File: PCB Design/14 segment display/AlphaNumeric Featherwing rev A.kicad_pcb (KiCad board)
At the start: 16 copper layers, 50.8 x 30.5 mm, 3 parts

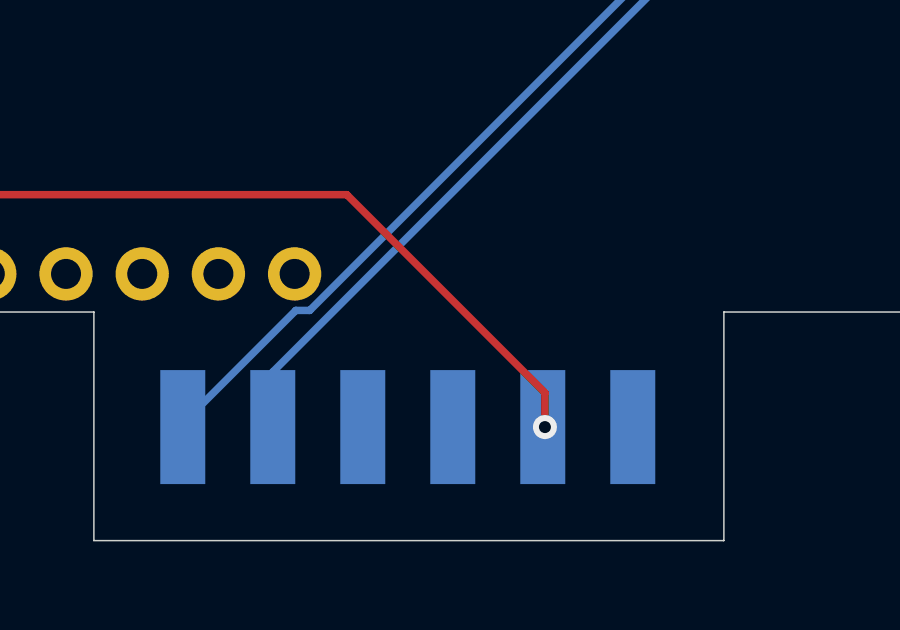
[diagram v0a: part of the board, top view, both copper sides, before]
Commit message: move vias off pads
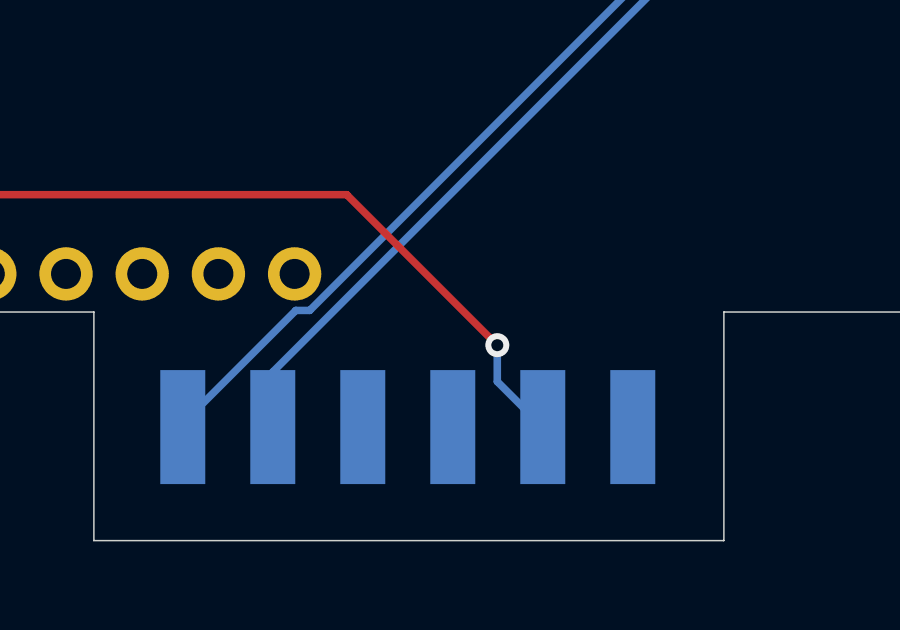
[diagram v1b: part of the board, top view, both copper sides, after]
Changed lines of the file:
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@@
   (segment (start 146.431 112.522) (end 134.6327 112.522) (width 0.25) (layer "F.Cu") (net 1))
   (segment (start 134.6327 112.522) (end 131.9911 115.1636) (width 0.25) (layer "F.Cu") (net 1))
-  (segment (start 153.035 120.269) (end 153.035 119.126) (width 0.25) (layer "F.Cu") (net 1))
-  (segment (start 153.035 119.126) (end 146.431 112.522) (width 0.25) (layer "F.Cu") (net 1))
-  (via (at 153.035 120.269) (size 0.8) (drill 0.4) (layers "F.Cu" "B.Cu") (net 1))
+  (segment (start 151.4475 117.5385) (end 146.431 112.522) (width 0.25) (layer "F.Cu") (net 1))
+  (via (at 151.4475 117.5385) (size 0.8) (drill 0.4) (layers "F.Cu" "B.Cu") (net 1))
+  (segment (start 152.963 120.269) (end 151.4475 118.7535) (width 0.25) (layer "B.Cu") (net 1))
+  (segment (start 151.4475 118.7535) (end 151.4475 117.5385) (width 0.25) (layer "B.Cu") (net 1))
   (segment (start 144.7312 116.3808) (end 145.195281 116.3808) (width 0.25) (layer "B.Cu") (net 14))
   (segment (start 140.963 120.149) (end 144.7312 116.3808) (width 0.25) (layer "B.Cu") (net 14))
